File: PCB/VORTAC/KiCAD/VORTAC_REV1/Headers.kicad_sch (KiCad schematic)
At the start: 7 parts, among them J1 DEBUG, J14 918-418K2023S40001, J15 STEPPER, J3 Conn_01x05

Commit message: Wayollaaaaa
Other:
- moved on the sheet: J1
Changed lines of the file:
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@@
 	(polyline
 		(pts
-			(xy 16.51 132.08) (xy 16.51 93.98)
+			(xy 16.51 133.35) (xy 16.51 93.98)
 		)
 		(stroke
@@
 	(polyline
 		(pts
-			(xy 60.96 93.98) (xy 60.96 132.08)
+			(xy 82.55 93.98) (xy 82.55 133.35)
 		)
 		(stroke
@@
 	(polyline
 		(pts
-			(xy 60.96 93.98) (xy 16.51 93.98)
+			(xy 82.55 93.98) (xy 16.51 93.98)
 		)
 		(stroke
@@
 	(wire
 		(pts
-			(xy 36.83 63.5) (xy 39.37 63.5)
-		)
-		(stroke
-			(width 0)
-			(type default)
-		)
-	)
-	(wire
-		(pts
-			(xy 54.61 68.58) (xy 52.07 68.58)
+			(xy 38.1 57.15) (xy 40.64 57.15)
+		)
+		(stroke
+			(width 0)
+			(type default)
+		)
+	)
+	(wire
+		(pts
+			(xy 55.88 62.23) (xy 53.34 62.23)
 		)
 		(stroke
@@
 	(wire
 		(pts
-			(xy 52.07 63.5) (xy 54.61 63.5)
-		)
-		(stroke
-			(width 0)
-			(type default)
-		)
-	)
-	(wire
-		(pts
-			(xy 39.37 66.04) (xy 36.83 66.04)
+			(xy 53.34 57.15) (xy 55.88 57.15)
+		)
+		(stroke
+			(width 0)
+			(type default)
+		)
+	)
+	(wire
+		(pts
+			(xy 40.64 59.69) (xy 38.1 59.69)
 		)
 		(stroke
@@
 	(wire
 		(pts
-			(xy 52.07 66.04) (xy 54.61 66.04)
+			(xy 53.34 59.69) (xy 55.88 59.69)
 		)
 		(stroke
@@
 	(polyline
 		(pts
-			(xy 16.51 132.08) (xy 60.96 132.08)
+			(xy 16.51 133.35) (xy 82.55 133.35)
 		)
 		(stroke
@@
 	(wire
 		(pts
-			(xy 36.83 68.58) (xy 39.37 68.58)
+			(xy 38.1 62.23) (xy 40.64 62.23)
 		)
 		(stroke
@@
 	(text "Debug Header"
 		(exclude_from_sim no)
-		(at 31.75 53.34 0)
+		(at 20.574 50.546 0)
 		(effects
 			(font
@@
 	(global_label "BOOT_1"
 		(shape input)
-		(at 54.61 68.58 0)
+		(at 55.88 62.23 0)
 		(effects
 			(font
@@
 		)
 		(property "Intersheetrefs" "${INTERSHEET_REFS}"
-			(at 54.61 68.58 0)
+			(at 55.88 62.23 0)
 			(effects
 				(font
@@
 	(global_label "DEBUG_SWDIO"
 		(shape input)
-		(at 54.61 63.5 0)
+		(at 55.88 57.15 0)
 		(effects
 			(font
@@
 		)
 		(property "Intersheetrefs" "${INTERSHEET_REFS}"
-			(at 54.61 63.5 0)
+			(at 55.88 57.15 0)
 			(effects
 				(font
@@
 	(global_label "NRST"
 		(shape input)
-		(at 54.61 66.04 0)
+		(at 55.88 59.69 0)
 		(effects
 			(font
@@
 		)
 		(property "Intersheetrefs" "${INTERSHEET_REFS}"
-			(at 54.61 66.04 0)
+			(at 55.88 59.69 0)
 			(effects
 				(font
@@
 	(global_label "DEBUG_SWO"
 		(shape input)
-		(at 60.96 74.93 0)
+		(at 62.23 68.58 0)
 		(effects
 			(font
@@
 		)
 		(property "Intersheetrefs" "${INTERSHEET_REFS}"
-			(at 60.96 74.93 0)
+			(at 62.23 68.58 0)
 			(effects
 				(font
@@
 	(global_label "DEBUG_SWCLK"
 		(shape input)
-		(at 36.83 63.5 180)
+		(at 38.1 57.15 180)
 		(effects
 			(font
@@
 		)
 		(property "Intersheetrefs" "${INTERSHEET_REFS}"
-			(at 36.83 63.5 0)
+			(at 38.1 57.15 0)
 			(effects
 				(font
@@
 	(symbol
 		(lib_id "Connector_Generic:Conn_02x03_Odd_Even")
-		(at 46.99 66.04 180)
+		(at 48.26 59.69 180)
 		(unit 1)
 		(exclude_from_sim no)
@@
 		(dnp no)
 		(property "Reference" "J1"
-			(at 53.34 76.2 0)
+			(at 54.61 69.85 0)
 			(effects
 				(font
@@
 		)
 		(property "Value" "DEBUG"
-			(at 53.34 73.66 0)
+			(at 54.61 67.31 0)
 			(effects
 				(font
@@
 		)
 		(property "Footprint" "ToolChanger:PinHeader_2x03_P1.27mm_Vertical"
-			(at 46.99 66.04 0)
+			(at 48.26 59.69 0)
 			(effects
 				(font
@@
 		)
 		(property "Datasheet" "~"
-			(at 46.99 66.04 0)
+			(at 48.26 59.69 0)
 			(effects
 				(font
@@
 		)
 		(property "Description" "Generic connector, double row, 02x03, odd/even pin numbering scheme (row 1 odd numbers, row 2 even numbers), script generated (kicad-library-utils/schlib/autogen/connector/)"
-			(at 46.99 66.04 0)
+			(at 48.26 59.69 0)
 			(effects
 				(font
@@
 	(symbol
 		(lib_id "VORTAC-rescue:+3.3V-power")
-		(at 36.83 68.58 90)
+		(at 38.1 62.23 90)
 		(unit 1)
 		(exclude_from_sim no)
@@
 		(dnp no)
 		(property "Reference" "#PWR0160"
-			(at 40.64 68.58 0)
+			(at 41.91 62.23 0)
 			(effects
 				(font
@@
 		)
 		(property "Value" "+3V3"
-			(at 33.5788 68.199 90)
+			(at 34.8488 61.849 90)
 			(effects
 				(font
@@
 		)
 		(property "Footprint" ""
-			(at 36.83 68.58 0)
+			(at 38.1 62.23 0)
 			(effects
 				(font
@@
 		)
 		(property "Datasheet" ""
-			(at 36.83 68.58 0)
+			(at 38.1 62.23 0)
 			(effects
 				(font
@@
 		)
 		(property "Description" ""
-			(at 36.83 68.58 0)
+			(at 38.1 62.23 0)
 			(effects
 				(font
@@
 	(symbol
 		(lib_id "VORTAC-rescue:GND-power")
-		(at 36.83 66.04 270)
+		(at 38.1 59.69 270)
 		(unit 1)
 		(exclude_from_sim no)
@@
 		(dnp no)
 		(property "Reference" "#PWR0161"
-			(at 30.48 66.04 0)
+			(at 31.75 59.69 0)
 			(effects
 				(font
@@
 		)
 		(property "Value" "GND"
-			(at 33.5788 66.167 90)
+			(at 34.8488 59.817 90)
 			(effects
 				(font
@@
 		)
 		(property "Footprint" ""
-			(at 36.83 66.04 0)
+			(at 38.1 59.69 0)
 			(effects
 				(font
@@
 		)
 		(property "Datasheet" ""
-			(at 36.83 66.04 0)
+			(at 38.1 59.69 0)
 			(effects
 				(font
@@
 		)
 		(property "Description" ""
-			(at 36.83 66.04 0)
-			(effects
-				(font
+			(at 38.1 59.69 0)
+			(effects
+				(font

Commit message: Fixed Library stuff
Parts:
- J1: footprint ToolChanger:PinHeader_2x03_P1.27mm_Vertical -> Vortac:PinHeader_2x03_P1.27mm_Vertical
- J14: footprint ToolChanger:USB-C-TH_HANBO_MC-118LD-H65 -> Vortac:USB-C-TH_HANBO_MC-118LD-H65
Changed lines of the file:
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@@
 			)
 		)
-		(property "Footprint" "ToolChanger:USB-C-TH_HANBO_MC-118LD-H65"
+		(property "Footprint" "Vortac:USB-C-TH_HANBO_MC-118LD-H65"
 			(at 35.56 166.37 0)
 			(effects
@@
 			)
 		)
-		(property "Footprint" "ToolChanger:PinHeader_2x03_P1.27mm_Vertical"
+		(property "Footprint" "Vortac:PinHeader_2x03_P1.27mm_Vertical"
 			(at 48.26 59.69 0)
 			(effects

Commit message: changed usb header
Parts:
- J14: footprint Vortac:USB-C-TH_HANBO_MC-118LD-H65 -> Vortac:USB-C-SMD_TYPEC-303-ACP16; LCSC C6332304 -> C720628
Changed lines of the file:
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@@
 			)
 		)
-		(property "Footprint" "Vortac:USB-C-TH_HANBO_MC-118LD-H65"
+		(property "Footprint" "Vortac:USB-C-SMD_TYPEC-303-ACP16"
 			(at 35.56 166.37 0)
 			(effects
@@
 			)
 		)
-		(property "Datasheet" "https://www.lcsc.com/datasheet/lcsc_datasheet_2412131142_Hanbo-Electronic-MC-118LD-H65_C6332304.pdf"
+		(property "Datasheet" "https://www.lcsc.com/datasheet/lcsc_datasheet_2411220120_XUNPU-TYPEC-303-ACP16_C720628.pdf"
 			(at 35.56 166.37 0)
 			(effects
@@
 			)
 		)
-		(property "LCSC" "C6332304"
+		(property "LCSC" "C720628"
 			(at 31.75 166.37 0)
 			(effects

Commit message: Liebe Griasse zurrueck
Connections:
- net DEBUG_SWO: now also J1.4 (Pin_4)
- net GND: no longer J1.4 (Pin_4)
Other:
- note added: "ESD Protection for Shield could be added (ther design add a cap and resistor to ground)"
- moved on the sheet: D5, J14, J3, R3, R4

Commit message: Gschenkle
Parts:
- added J2: DEBUG, symbol Connector_Generic:Conn_02x04_Odd_Even
- D5: footprint Diode_SMD:D_SOD-123 -> Diode_SMD:D_SOD-323
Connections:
- net BOOT_1: no longer J1.1 (Pin_1)
- new net BOOT_0: J1.1 (Pin_1)
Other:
- note added: "BOOT_1 optional for SRAM boot If not included a sjumper it could be accessed by soldering to the resistor when needed"
- note added: "ESD Protection for Shield could be added (other design add a cap and resistor to ground)"
- note removed: "ESD Protection for Shield could be added (ther design add a cap and resistor to ground)"
- moved on the sheet: J1
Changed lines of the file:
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@@
 	(wire
 		(pts
-			(xy 38.1 57.15) (xy 40.64 57.15)
-		)
-		(stroke
-			(width 0)
-			(type default)
-		)
-	)
-	(wire
-		(pts
-			(xy 55.88 62.23) (xy 53.34 62.23)
+			(xy 57.15 59.69) (xy 54.61 59.69)
+		)
+		(stroke
+			(width 0)
+			(type default)
+		)
+	)
+	(wire
+		(pts
+			(xy 39.37 54.61) (xy 41.91 54.61)
 		)
 		(stroke
@@
 	(wire
 		(pts
-			(xy 53.34 57.15) (xy 55.88 57.15)
-		)
-		(stroke
-			(width 0)
-			(type default)
-		)
-	)
-	(wire
-		(pts
-			(xy 40.64 59.69) (xy 38.1 59.69)
+			(xy 41.91 59.69) (xy 39.37 59.69)
+		)
+		(stroke
+			(width 0)
+			(type default)
+		)
+	)
+	(wire
+		(pts
+			(xy 54.61 57.15) (xy 57.15 57.15)
 		)
 		(stroke
@@
 	(wire
 		(pts
-			(xy 53.34 59.69) (xy 55.88 59.69)
+			(xy 41.91 57.15) (xy 39.37 57.15)
 		)
 		(stroke
@@
 	(wire
 		(pts
-			(xy 38.1 62.23) (xy 40.64 62.23)
+			(xy 57.15 54.61) (xy 54.61 54.61)
 		)
 		(stroke
@@
 		)
 	)
+	(text "BOOT_1 optional for SRAM boot\nIf not included a sjumper it could be \naccessed by soldering to the resistor when needed"
+		(exclude_from_sim no)
+		(at 103.632 52.832 0)
+		(effects
+			(font
+				(size 0.7874 0.7874)
+			)
+			(justify left top)
+		)
+	)
 	(text "Debug Header"
 		(exclude_from_sim no)
@@
 		)
 	)
-	(text "ESD Protection for Shield could be added\n(ther design add a cap and resistor to ground)"
+	(text "ESD Protection for Shield could be added\n(other design add a cap and resistor to ground)"
 		(exclude_from_sim no)
 		(at 20.32 188.468 0)
@@
 	(global_label "BOOT_1"
 		(shape input)
-		(at 55.88 62.23 0)
-		(effects
-			(font
-				(size 1.27 1.27)
-			)
-			(justify left)
+		(at 99.06 53.34 180)
+		(effects
+			(font
+				(size 1.27 1.27)
+			)
+			(justify right)
 		)
 		(property "Intersheetrefs" "${INTERSHEET_REFS}"
-			(at 55.88 62.23 0)
+			(at 99.06 53.34 0)
+			(effects
+				(font
+					(size 1.27 1.27)
+				)
+				(hide yes)
+			)
+		)
+	)
+	(global_label "BOOT_0"
+		(shape input)
+		(at 39.37 54.61 180)
+		(effects
+			(font
+				(size 1.27 1.27)
+			)
+			(justify right)
+		)
+		(property "Intersheetrefs" "${INTERSHEET_REFS}"
+			(at 39.37 54.61 0)
 			(effects
 				(font
@@
 	(global_label "DEBUG_SWDIO"
 		(shape input)
-		(at 55.88 57.15 0)
-		(effects
-			(font
-				(size 1.27 1.27)
-			)
-			(justify left)
+		(at 39.37 59.69 180)
+		(effects
+			(font
+				(size 1.27 1.27)
+			)
+			(justify right)
 		)
 		(property "Intersheetrefs" "${INTERSHEET_REFS}"
-			(at 55.88 57.15 0)
+			(at 39.37 59.69 0)
 			(effects
 				(font
@@
 	(global_label "NRST"
 		(shape input)
-		(at 55.88 59.69 0)
-		(effects
-			(font
-				(size 1.27 1.27)
-			)
-			(justify left)
+		(at 39.37 57.15 180)
+		(effects
+			(font
+				(size 1.27 1.27)
+			)
+			(justify right)
 		)
 		(property "Intersheetrefs" "${INTERSHEET_REFS}"
-			(at 55.88 59.69 0)
+			(at 39.37 57.15 0)
 			(effects
 				(font
@@
 	(global_label "DEBUG_SWO"
 		(shape input)
-		(at 38.1 59.69 180)
-		(effects
-			(font
-				(size 1.27 1.27)
-			)
-			(justify right)
+		(at 57.15 57.15 0)
+		(effects
+			(font
+				(size 1.27 1.27)
+			)
+			(justify left)
 		)
 		(property "Intersheetrefs" "${INTERSHEET_REFS}"
-			(at 38.1 59.69 0)
+			(at 57.15 57.15 0)
 			(effects
 				(font
@@
 	(global_label "DEBUG_SWCLK"
 		(shape input)
-		(at 38.1 57.15 180)
-		(effects
-			(font
-				(size 1.27 1.27)
-			)
-			(justify right)
+		(at 57.15 59.69 0)
+		(effects
+			(font
+				(size 1.27 1.27)
+			)
+			(justify left)
 		)
 		(property "Intersheetrefs" "${INTERSHEET_REFS}"
-			(at 38.1 57.15 0)
+			(at 57.15 59.69 0)
 			(effects
 				(font
@@
 			)
 		)
-		(property "Footprint" "Diode_SMD:D_SOD-123"
+		(property "Footprint" "Diode_SMD:D_SOD-323"
 			(at 55.88 140.97 0)
 			(effects
@@
 	(symbol
 		(lib_id "Connector_Generic:Conn_02x03_Odd_Even")
-		(at 48.26 59.69 180)
+		(at 46.99 57.15 0)
 		(unit 1)
 		(exclude_from_sim no)
@@
 		(dnp no)
 		(property "Reference" "J1"
-			(at 46.99 53.34 0)
+			(at 45.212 51.054 0)
 			(effects
 				(font
@@
 		)
 		(property "Value" "DEBUG"
-			(at 46.99 50.8 0)
+			(at 50.292 51.054 0)
 			(effects
 				(font
@@
 		)
 		(property "Footprint" "Vortac:PinHeader_2x03_P1.27mm_Vertical"
-			(at 48.26 59.69 0)
+			(at 46.99 57.15 0)
 			(effects
 				(font
@@
 		)
 		(property "Datasheet" "~"
-			(at 48.26 59.69 0)
+			(at 46.99 57.15 0)
 			(effects
 				(font
@@
 		)
 		(property "Description" "Generic connector, double row, 02x03, odd/even pin numbering scheme (row 1 odd numbers, row 2 even numbers), script generated (kicad-library-utils/schlib/autogen/connector/)"
-			(at 48.26 59.69 0)
+			(at 46.99 57.15 0)
 			(effects
 				(font
@@
 	(symbol
 		(lib_id "VORTAC-rescue:+3.3V-power")
-		(at 38.1 62.23 90)
+		(at 57.15 54.61 270)
 		(unit 1)
 		(exclude_from_sim no)
@@
 		(dnp no)
 		(property "Reference" "#PWR0160"
-			(at 41.91 62.23 0)
+			(at 53.34 54.61 0)
 			(effects
 				(font
@@
 		)
 		(property "Value" "+3V3"
-			(at 34.8488 61.849 90)
+			(at 60.4012 54.991 90)
 			(effects
 				(font
@@
 		)
 		(property "Footprint" ""
-			(at 38.1 62.23 0)
+			(at 57.15 54.61 0)
 			(effects
 				(font
@@
 		)
 		(property "Datasheet" ""
-			(at 38.1 62.23 0)
+			(at 57.15 54.61 0)
 			(effects
 				(font
@@
 		)
 		(property "Description" ""
-			(at 38.1 62.23 0)
+			(at 57.15 54.61 0)
 			(effects
 				(font
@@
 					(unit 1)
 				)
+			)
+		)
+	)
+	(symbol
+		(lib_id "Connector_Generic:Conn_02x04_Odd_Even")
+		(at 46.99 71.12 0)
+		(unit 1)
+		(exclude_from_sim no)
+		(in_bom yes)
+		(on_board yes)
+		(dnp no)
+		(property "Reference" "J2"
+			(at 46.228 64.516 0)
+			(effects
+				(font
+					(size 1.27 1.27)
+				)
+			)
+		)
+		(property "Value" "DEBUG"
+			(at 51.816 64.516 0)
+			(effects
+				(font
+					(size 1.27 1.27)
+				)
+			)
+		)
+		(property "Footprint" ""
+			(at 46.99 71.12 0)
+			(effects
+				(font
+					(size 1.27 1.27)
+				)
+				(hide yes)
+			)
+		)
+		(property "Datasheet" "~"
+			(at 46.99 71.12 0)
+			(effects
+				(font
+					(size 1.27 1.27)
+				)
+				(hide yes)
+			)
+		)
+		(property "Description" "Generic connector, double row, 02x04, odd/even pin numbering scheme (row 1 odd numbers, row 2 even numbers), script generated (kicad-library-utils/schlib/autogen/connector/)"
+			(at 46.99 71.12 0)
+			(effects
+				(font
+					(size 1.27 1.27)
+				)
+				(hide yes)
+			)
+		)
+		(pin "2"
+		)
+		(pin "1"
+		)
+		(pin "6"
+		)
+		(pin "7"
+		)
+		(pin "4"
+		)
+		(pin "3"
+		)
+		(pin "5"
+		)
+		(pin "8"
+		)
+		(instances
+			(project "VORTAC_REV1"
+				(path "/ed58d858-d9f9-4504-a982-ccfc7f9efbad/00000000-0000-0000-0000-0000613db78d"
+					(reference "J2")
+					(unit 1)
+				)

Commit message: Hallo
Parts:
- J15: footprint Connector_JST:JST_PH_B4B-PH-K_1x04_P2.00mm_Vertical -> Vortac:JST_PH_S4B-PH-K_1x04_P2.00mm_Horizontal
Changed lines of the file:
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@@
 			)
 		)
-		(property "Footprint" "Connector_JST:JST_PH_B4B-PH-K_1x04_P2.00mm_Vertical"
+		(property "Footprint" "Vortac:JST_PH_S4B-PH-K_1x04_P2.00mm_Horizontal"
 			(at 48.26 29.21 0)
 			(effects

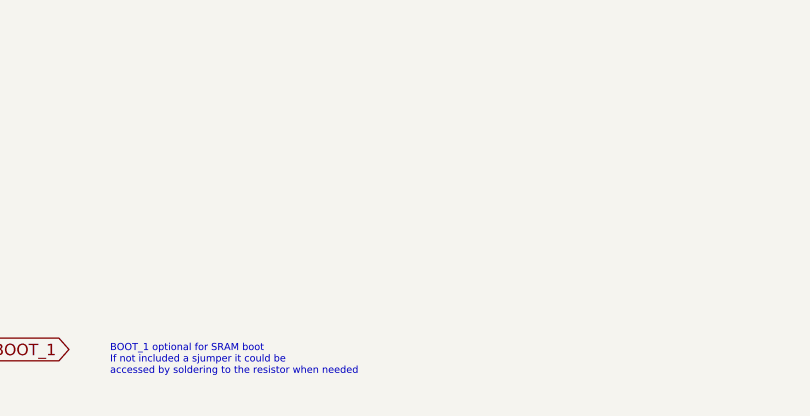
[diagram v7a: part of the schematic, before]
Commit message: Schematic updates
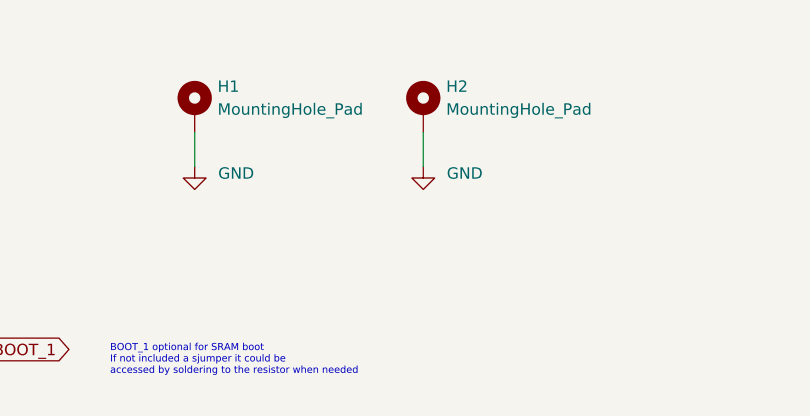
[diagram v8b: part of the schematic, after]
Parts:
- added H1, H2: MountingHole_Pad, MountingHole:MountingHole_2.2mm_M2_Pad_Via, symbol Mechanical:MountingHole_Pad
- J3: footprint Connector_PinHeader_2.54mm:PinHeader_1x05_P2.54mm_Vertical -> Connector_PinHeader_2.54mm:PinHeader_2x03_P2.54mm_Vertical
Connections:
- net GND: now also H1.1, H2.1
